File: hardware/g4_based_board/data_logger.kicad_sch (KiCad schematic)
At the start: 14 parts, among them J1 Conn_01x07_Socket, J2 Conn_02x07_Odd_Even, J3 Conn_01x07_Socket, J39 Conn_01x03

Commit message: rev-1
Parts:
- added J13: Conn_01x09_Pin, Connector_PinHeader_2.54mm:PinHeader_1x09_P2.54mm_Vertical, symbol Connector:Conn_01x09_Pin
- added J40: Conn_01x07_Socket, Connector_PinHeader_2.54mm:PinHeader_1x07_P2.54mm_Vertical, symbol Connector:Conn_01x07_Socket
- added J43: Conn_01x06, Connector_PinHeader_2.54mm:PinHeader_1x06_P2.54mm_Vertical, symbol Connector_Generic:Conn_01x06
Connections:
- net +3.3V: now also J2.1 (Pin_1), J2.2 (Pin_2), J40.2 (Pin_2); no longer J2.3 (Pin_3), J2.4 (Pin_4)
- net +5P: now also J40.1 (Pin_1)
- net +5V: now also J2.3 (Pin_3), J2.4 (Pin_4); no longer J2.1 (Pin_1), J2.2 (Pin_2)
- net +BATT: now also J2.10 (Pin_10), J2.9 (Pin_9), J40.3 (Pin_3); no longer J2.5 (Pin_5), J2.6 (Pin_6)
- net +VDC: now also J40.4 (Pin_4)
- net -VDC: now also J2.5 (Pin_5), J2.6 (Pin_6), J40.5 (Pin_5); no longer J2.10 (Pin_10), J2.9 (Pin_9)
- net GND: now also J40.6 (Pin_6), J40.7 (Pin_7)
- net mcu/USART_RX: now also J39.3 (Pin_3); no longer J39.2 (Pin_2)
- net mcu/USART_TX: now also J39.2 (Pin_2); no longer J39.3 (Pin_3)
- new net mcu/ADC-GPIO-PWM-1-DIFF1-1: J13.7 (Pin_7)
- new net mcu/ADC-GPIO-PWM-10: J13.3 (Pin_3)
- new net mcu/ADC-GPIO-PWM-12: J13.2 (Pin_2)
- new net mcu/ADC-GPIO-PWM-2-DIFF1-2: J13.6 (Pin_6)
- new net mcu/ADC-GPIO-PWM-3: J13.5 (Pin_5)
- new net mcu/ADC-GPIO-PWM-4: J13.4 (Pin_4)
- new net mcu/ADC-GPIO-PWM-9: J13.1 (Pin_1)
- new net mcu/DAC1_OUT-ADC-GPIO-PWM: J13.8 (Pin_8)
- new net mcu/DAC2_OUT-ADC-GPIO-PWM: J13.9 (Pin_9)
- new net mcu/DIGITAL_IO_EN_1: J43.1 (Pin_1)
- new net mcu/DIGITAL_IO_EN_2: J43.2 (Pin_2)
- new net mcu/DIGITAL_IO_EN_3: J43.3 (Pin_3)
- new net mcu/DIGITAL_IO_EN_4: J43.4 (Pin_4)
- new net mcu/DIGITAL_IO_EN_5: J43.5 (Pin_5)
- new net mcu/DIGITAL_IO_EN_6: J43.6 (Pin_6)
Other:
- added sheet analog_in (analog_in.kicad_sch)
- added sheet power_amp (power_amp.kicad_sch)
- note added: "THIS IS NOT ON THE BOARD DUE TO SPACE"

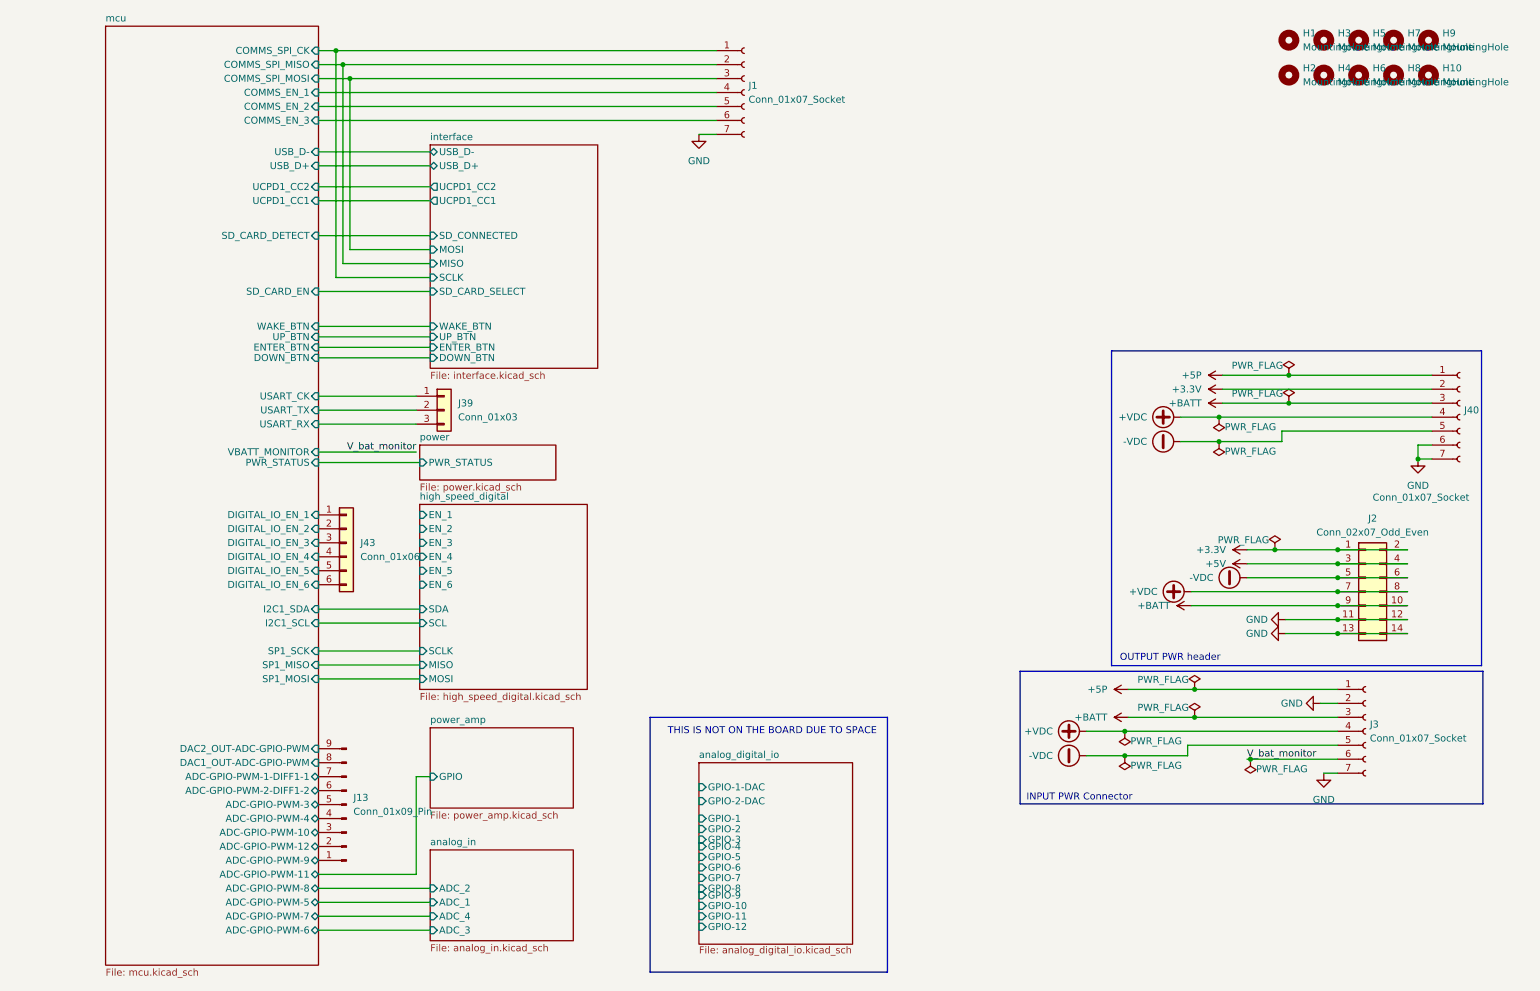
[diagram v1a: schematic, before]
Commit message: minor addtion and swd header added and usart removed
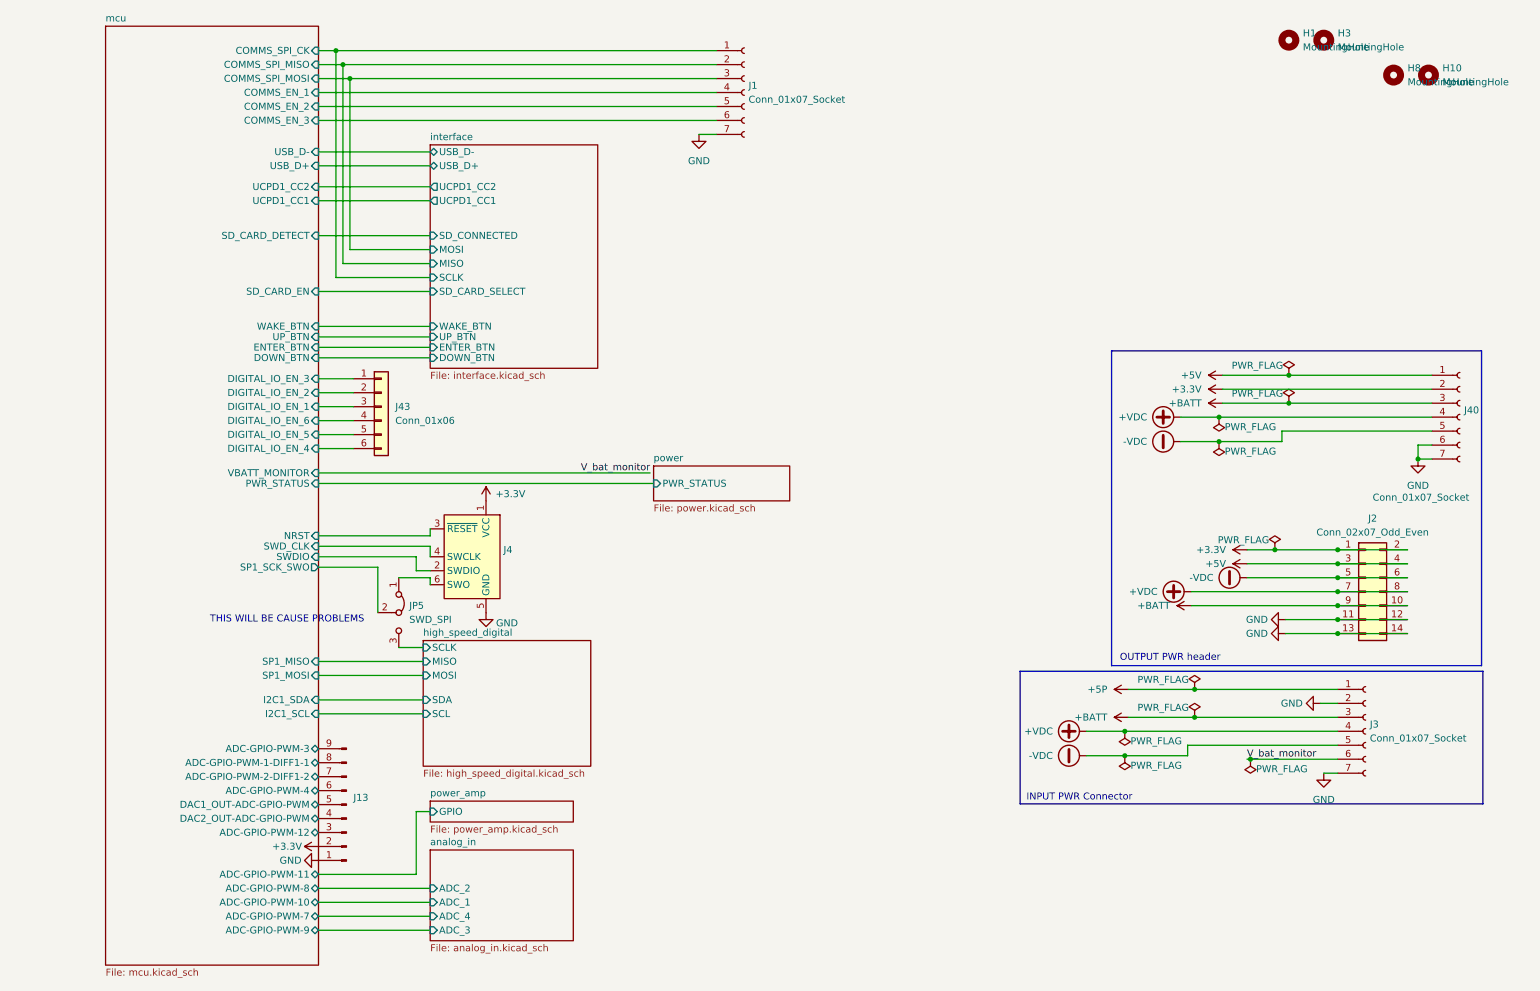
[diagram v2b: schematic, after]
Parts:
- removed H2, H4, H5, H6, H7, H9: MountingHole, MountingHole:MountingHole_3.2mm_M3, symbol Mechanical:MountingHole
- removed J39: Conn_01x03, Connector_PinHeader_2.54mm:PinHeader_1x03_P2.54mm_Vertical, symbol Connector_Generic:Conn_01x03
- added J4: Conn_ARM_SWD_TagConnect_TC2030-NL, Connector:Tag-Connect_TC2030-IDC-NL_2x03_P1.27mm_Vertical, symbol Connector:Conn_ARM_SWD_TagConnect_TC2030-NL
- added JP5: SWD_SPI, Jumper:SolderJumper-3_P1.3mm_Bridged2Bar12_RoundedPad1.0x1.5mm, symbol Jumper:Jumper_3_Bridged12
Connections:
- net mcu/ADC-GPIO-PWM-10 is gone; now on net mcu/ADC-GPIO-PWM-12: J13.3 (Pin_3)
- net mcu/ADC-GPIO-PWM-9 is gone; now on net GND: J13.1 (Pin_1)
- net +3.3V: now also J13.2 (Pin_2), J4.1 (VCC)
- net +5P: no longer J40.1 (Pin_1)
- net +5V: now also J40.1 (Pin_1)
- net GND: now also J4.5 (GND)
- net high_speed_digital/SCLK: now also JP5.3 (B)
- net mcu/ADC-GPIO-PWM-1-DIFF1-1: now also J13.8 (Pin_8); no longer J13.7 (Pin_7)
- net mcu/ADC-GPIO-PWM-12: no longer J13.2 (Pin_2)
- net mcu/ADC-GPIO-PWM-2-DIFF1-2: now also J13.7 (Pin_7); no longer J13.6 (Pin_6)
- net mcu/ADC-GPIO-PWM-3: now also J13.9 (Pin_9); no longer J13.5 (Pin_5)
- net mcu/ADC-GPIO-PWM-4: now also J13.6 (Pin_6); no longer J13.4 (Pin_4)
- net mcu/DAC1_OUT-ADC-GPIO-PWM: now also J13.5 (Pin_5); no longer J13.8 (Pin_8)
- net mcu/DAC2_OUT-ADC-GPIO-PWM: now also J13.4 (Pin_4); no longer J13.9 (Pin_9)
- net mcu/DIGITAL_IO_EN_1: now also J43.3 (Pin_3); no longer J43.1 (Pin_1)
- net mcu/DIGITAL_IO_EN_3: now also J43.1 (Pin_1); no longer J43.3 (Pin_3)
- net mcu/DIGITAL_IO_EN_4: now also J43.6 (Pin_6); no longer J43.4 (Pin_4)
- net mcu/DIGITAL_IO_EN_6: now also J43.4 (Pin_4); no longer J43.6 (Pin_6)
- new net: J4.6 (SWO), JP5.1 (A)
- new net mcu/NRST: J4.3 (~{RESET})
- new net mcu/SP1_SCK_SWO: JP5.2 (C)
- new net mcu/SWDIO: J4.2 (SWDIO)
- new net mcu/SWD_CLK: J4.4 (SWCLK)
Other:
- removed sheet analog_digital_io
- sheet high_speed_digital ports: added none; removed EN_1, EN_2, EN_3, EN_4, EN_5, EN_6
- sheet mcu ports: added NRST, SP1_SCK_SWO, SWDIO, SWD_CLK; removed ADC-GPIO-PWM-5, ADC-GPIO-PWM-6, SP1_SCK, USART_CK, USART_RX, USART_TX
- note added: "THIS WILL BE CAUSE PROBLEMS"
- note removed: "THIS IS NOT ON THE BOARD DUE TO SPACE"
- moved on the sheet: J43

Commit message: upadate to reflect larger changes
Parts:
- removed H1, H10, H3, H8: MountingHole, MountingHole:MountingHole_3.2mm_M3, symbol Mechanical:MountingHole
- removed J13: Conn_01x09_Pin, Connector_PinHeader_2.54mm:PinHeader_1x09_P2.54mm_Vertical, symbol Connector:Conn_01x09_Pin
- removed J2: Conn_02x07_Odd_Even, Connector_PinHeader_2.54mm:PinHeader_2x07_P2.54mm_Vertical, symbol Connector_Generic:Conn_02x07_Odd_Even
- removed J43: Conn_01x06, Connector_PinHeader_2.54mm:PinHeader_1x06_P2.54mm_Vertical, symbol Connector_Generic:Conn_01x06
- added H1, H2, H3, H4: MountingHole_Pad, MountingHole:MountingHole_3.2mm_M3_DIN965_Pad_TopOnly, symbol Mechanical:MountingHole_Pad
- added J2: Conn_01x07_Socket, Connector_PinHeader_2.54mm:PinHeader_1x07_P2.54mm_Vertical, symbol Connector:Conn_01x07_Socket
- added J7: Conn_01x10, Connector_PinHeader_2.54mm:PinHeader_1x10_P2.54mm_Vertical, symbol Connector_Generic:Conn_01x10
- added TP4, TP5, TP6: TestPoint, TestPoint:TestPoint_Pad_2.0x2.0mm, symbol Connector:TestPoint
- J4: footprint Connector:Tag-Connect_TC2030-IDC-NL_2x03_P1.27mm_Vertical -> Connector:Tag-Connect_TC2030-IDC-FP_2x03_P1.27mm_Vertical
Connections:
- net +3.3V: now also J40.3 (Pin_3), J2.3 (Pin_3), J7.2 (Pin_2); no longer J40.2 (Pin_2)
- net +5V: now also J40.7 (Pin_7), J2.7 (Pin_7); no longer J40.1 (Pin_1)
- net +BATT: now also J40.4 (Pin_4), J2.6 (Pin_6); no longer J40.3 (Pin_3)
- net +VDC: now also J40.5 (Pin_5), J2.5 (Pin_5); no longer J40.4 (Pin_4)
- net -VDC: now also J40.6 (Pin_6), J2.4 (Pin_4); no longer J40.5 (Pin_5)
- net GND: now also J40.1 (Pin_1), J40.2 (Pin_2), J2.1 (Pin_1), J2.2 (Pin_2), J7.1 (Pin_1), J7.10 (Pin_10); no longer J40.6 (Pin_6), J40.7 (Pin_7)
- net mcu/ADC-GPIO-PWM-1-DIFF1-1: now also J7.7 (Pin_7)
- net mcu/ADC-GPIO-PWM-3: now also TP5.1
- net mcu/DAC1_OUT-ADC-GPIO-PWM: now also J7.8 (Pin_8)
- net mcu/DAC2_OUT-ADC-GPIO-PWM: now also J7.9 (Pin_9)
- net mcu/DIGITAL_IO_EN_3: now also TP6.1
- net mcu/DIGITAL_IO_EN_5: now also TP4.1
- new net GNDS: H1.1, H2.1, H3.1, H4.1
- new net mcu/ADC-GPIO-PWM-10: J7.6 (Pin_6)
- new net mcu/ADC-GPIO-PWM-7: J7.3 (Pin_3)
- new net mcu/ADC-GPIO-PWM-8: J7.4 (Pin_4)
- new net mcu/ADC-GPIO-PWM-9: J7.5 (Pin_5)
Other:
- sheet high_speed_digital ports: added BTN_1, BTN_2, BTN_3, BTN_4, CAMERA_POWER_EN, CS, HI_POWER_EN; removed none
- sheet interface ports: added none; removed DOWN_BTN, ENTER_BTN, UP_BTN, WAKE_BTN
- sheet mcu ports: added PWM_1, PWM_2; removed DIGITAL_IO_EN_4
- sheet power_amp ports: added GPIO_0, GPIO_1; removed GPIO
- note added: "there are no good ways to route these"
- moved on the sheet: J4, JP5
